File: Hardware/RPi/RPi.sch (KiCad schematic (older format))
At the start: 90 parts, among them P1 USB_B, P10 Solder_Pad, P11 Solder_Pad, P12 Solder_Pad, P13 Solder_Pad, P14 Solder_Pad, P15 Solder_Pad, P16 Solder_Pad, P17 Solder_Pad, P18 Solder_Pad, P2 USB_A, P3 USB_A, P4 USB_A, P5 USB_A, P6 Solder_Pad, P7 Solder_Pad, P8 Solder_Pad, P9 Solder_Pad, U1 AP1117E25, U10 WS2812B, U11 WS2812B, U12 WS2812B, U13 Teensy_LC, U14 WS2812B, U15 WS2812B, U16 WS2812B, U17 WS2812B, U18 WS2812B, U19 WS2812B, U2 Dual_buffer_NC7WZ16, U3 FE1.1s, U4 MPU_9150, U5 RPi_Interface, U6 ESP-12E, U7 WS2812B, U8 WS2812B, U9 WS2812B, Y1 Crystal 12MHz

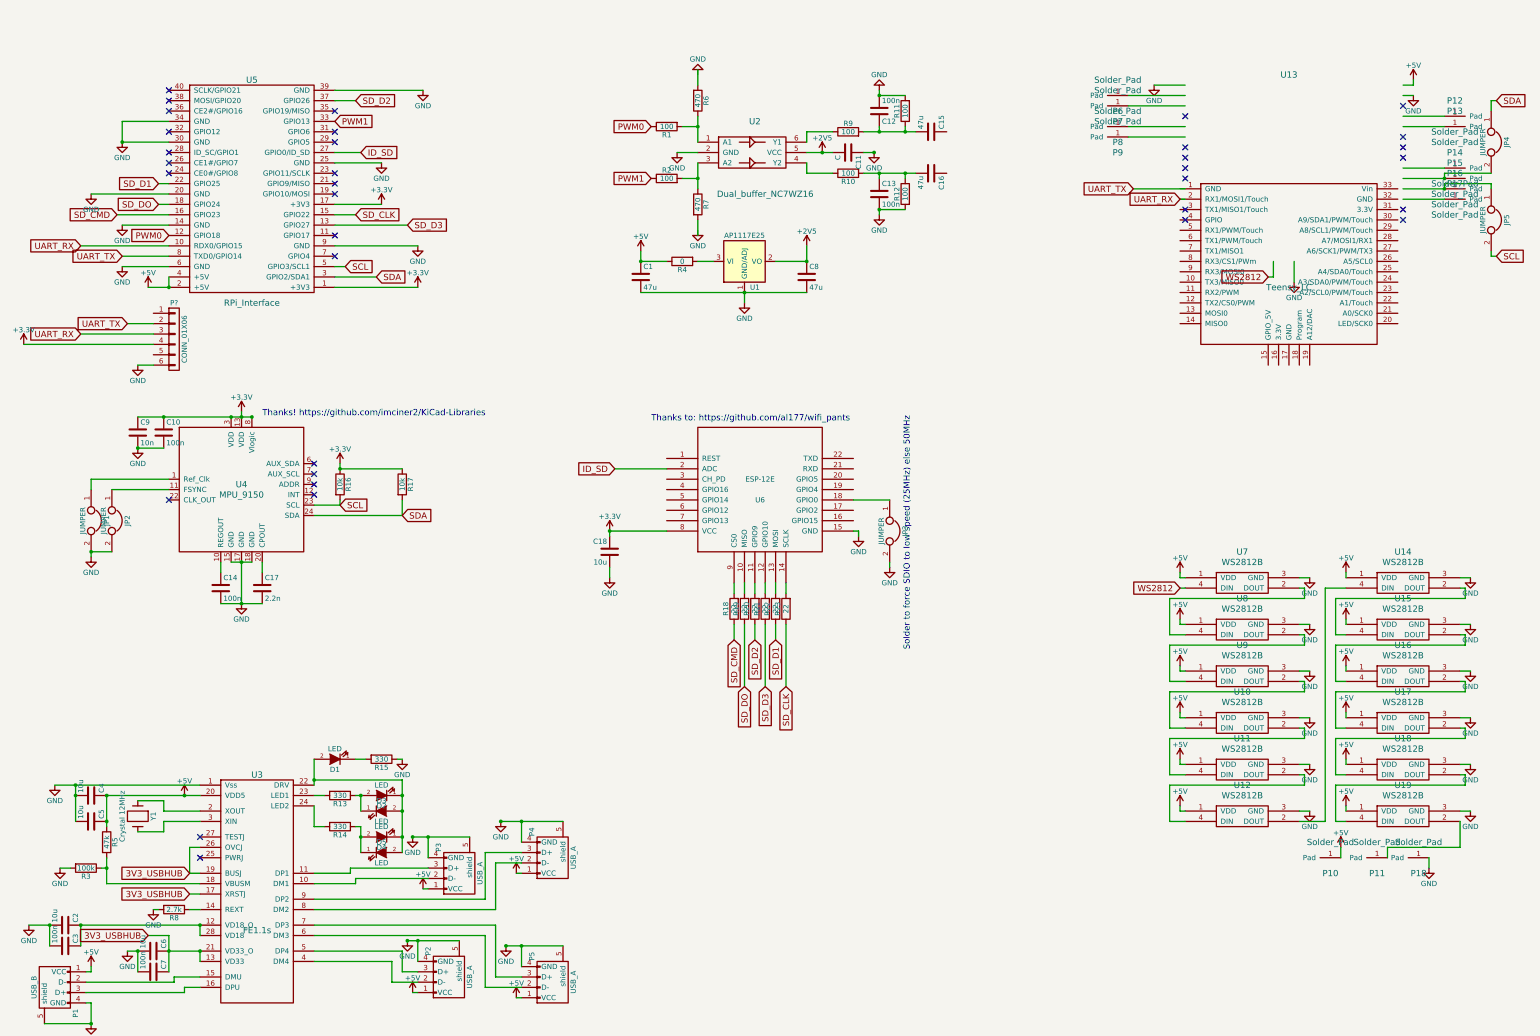
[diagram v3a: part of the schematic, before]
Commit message: Creating footprints
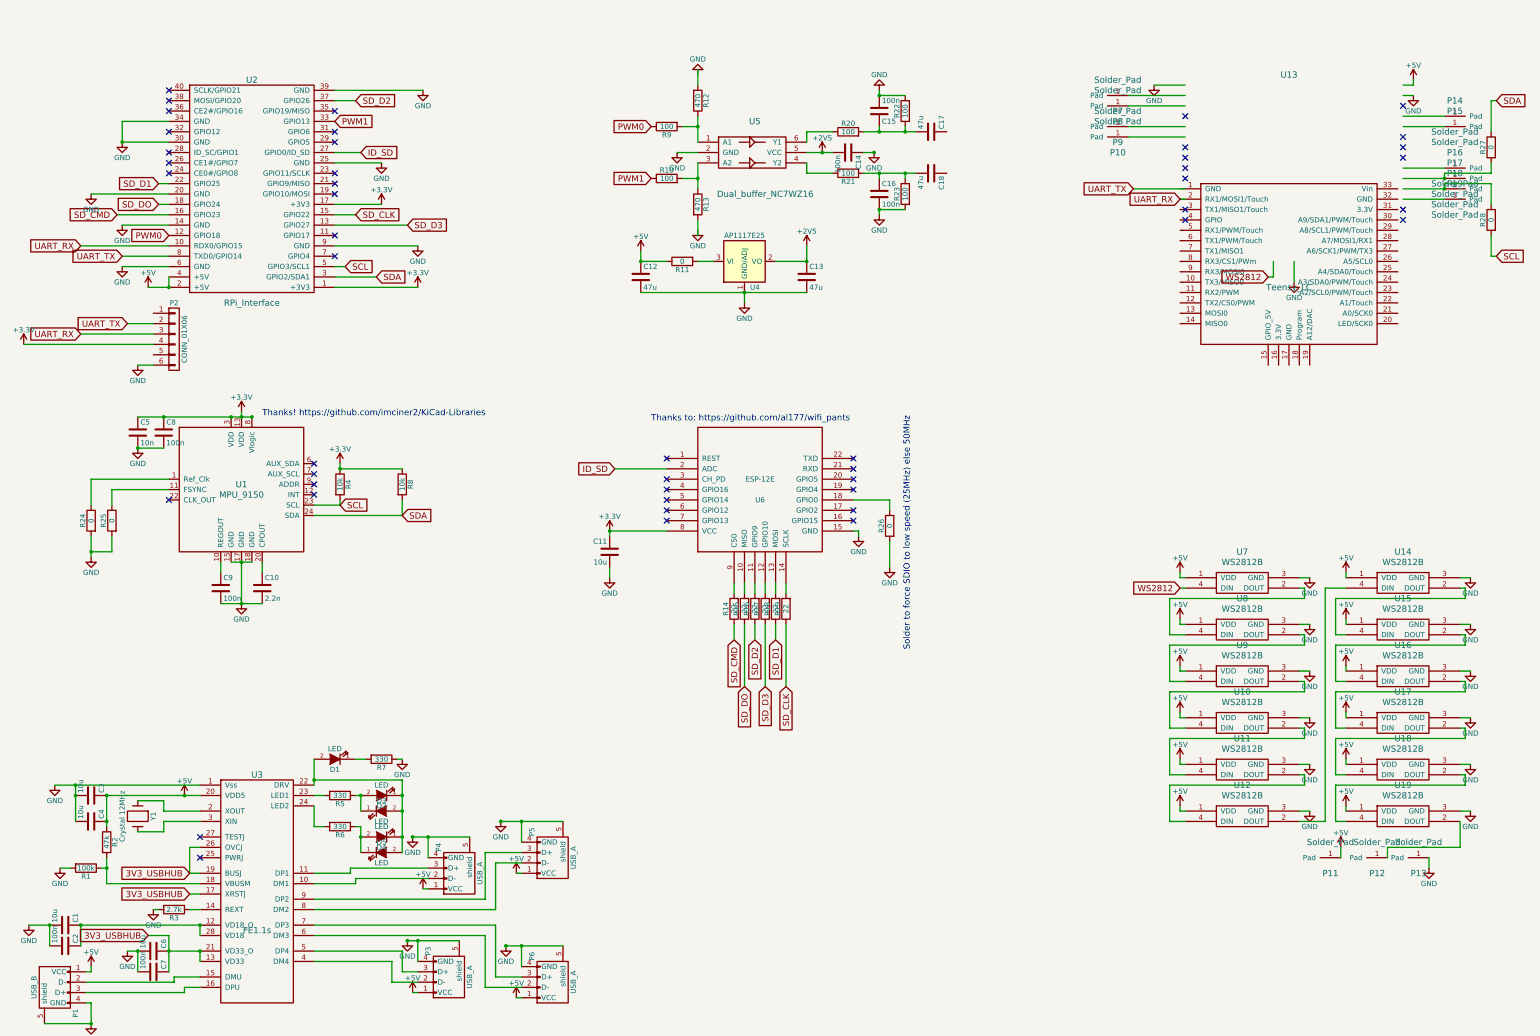
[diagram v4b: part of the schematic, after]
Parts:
- removed JP1, JP2, JP3, JP4, JP5: JUMPER, symbol JUMPER
- added R24, R25, R26, R27, R28: 0, Resistors_SMD:R_0603, symbol R
- C10: renamed from C17; footprint (none) -> Capacitors_SMD:C_0603
- C11: renamed from C18; footprint (none) -> Capacitors_SMD:C_0603
- C12: renamed from C1; footprint (none) -> Capacitors_SMD:C_0805
- C13: renamed from C8; footprint (none) -> Capacitors_SMD:C_0805
- C14: renamed from C11; value C -> 100n; footprint (none) -> Capacitors_SMD:C_0603
- C15: renamed from C12; footprint (none) -> Capacitors_SMD:C_0603
- C16: renamed from C13; footprint (none) -> Capacitors_SMD:C_0603
- C17: renamed from C15; footprint (none) -> Capacitors_SMD:C_0805
- C18: renamed from C16; footprint (none) -> Capacitors_SMD:C_0805
- C2: renamed from C3; footprint (none) -> Capacitors_SMD:C_0603
- C3: renamed from C4; footprint (none) -> Capacitors_SMD:C_0603
- C4: renamed from C5; footprint (none) -> Capacitors_SMD:C_0603
- C5: renamed from C9; footprint (none) -> Capacitors_SMD:C_0603
- C6, C7: footprint (none) -> Capacitors_SMD:C_0603
- C8: renamed from C10; footprint (none) -> Capacitors_SMD:C_0603
- C9: renamed from C14; footprint (none) -> Capacitors_SMD:C_0603
- D1, D2, D3, D4, D5: footprint (none) -> LEDs:LED_0603
- P1: footprint (none) -> Connect:USB_Mini-B
- P10: renamed from P9; footprint (none) -> Measurement_Points:Measurement_Point_Square-SMD-Pad_Big
- P11: renamed from P10; footprint (none) -> Measurement_Points:Measurement_Point_Square-SMD-Pad_Big
- P12: renamed from P11; footprint (none) -> Measurement_Points:Measurement_Point_Square-SMD-Pad_Big
- P13: renamed from P18; footprint (none) -> Measurement_Points:Measurement_Point_Square-SMD-Pad_Big
- P14: renamed from P12; footprint (none) -> Measurement_Points:Measurement_Point_Square-SMD-Pad_Big
- P15: renamed from P13; footprint (none) -> Measurement_Points:Measurement_Point_Square-SMD-Pad_Big
- P16: renamed from P14; footprint (none) -> Measurement_Points:Measurement_Point_Square-SMD-Pad_Big
- P17: renamed from P15; footprint (none) -> Measurement_Points:Measurement_Point_Square-SMD-Pad_Big
- P18: renamed from P16; footprint (none) -> Measurement_Points:Measurement_Point_Square-SMD-Pad_Big
- P19: renamed from P17; footprint (none) -> Measurement_Points:Measurement_Point_Square-SMD-Pad_Big
- P2: renamed from P?; footprint (none) -> TimeArc:1x06 pinheader smd
- P7: renamed from P6; footprint (none) -> Measurement_Points:Measurement_Point_Square-SMD-Pad_Big
- P8: renamed from P7; footprint (none) -> Measurement_Points:Measurement_Point_Square-SMD-Pad_Big
- P9: renamed from P8; footprint (none) -> Measurement_Points:Measurement_Point_Square-SMD-Pad_Big
- R1: renamed from R3; footprint (none) -> Resistors_SMD:R_0603
- R10: renamed from R2; footprint (none) -> Resistors_SMD:R_0603
- R11: renamed from R4; footprint (none) -> Resistors_SMD:R_0603
- R12: renamed from R6; footprint (none) -> Resistors_SMD:R_0603
- R13: renamed from R7; footprint (none) -> Resistors_SMD:R_0603
- R14: renamed from R18; footprint (none) -> Resistors_SMD:R_0603
- R15: renamed from R19; footprint (none) -> Resistors_SMD:R_0603
- R16: renamed from R20; footprint (none) -> Resistors_SMD:R_0603
- R17: renamed from R21; footprint (none) -> Resistors_SMD:R_0603
- R18: renamed from R22; footprint (none) -> Resistors_SMD:R_0603
- R19: renamed from R23; footprint (none) -> Resistors_SMD:R_0603
- R2: renamed from R5; footprint (none) -> Resistors_SMD:R_0603
- R20: renamed from R9; footprint (none) -> Resistors_SMD:R_0603
- R21: renamed from R10; footprint (none) -> Resistors_SMD:R_0603
- R22: renamed from R11; footprint (none) -> Resistors_SMD:R_0603
- R23: renamed from R12; footprint (none) -> Resistors_SMD:R_0603
- R3: renamed from R8; footprint (none) -> Resistors_SMD:R_0603
- R4: renamed from R16; footprint (none) -> Resistors_SMD:R_0603
- R5: renamed from R13; footprint (none) -> Resistors_SMD:R_0603
- R6: renamed from R14; footprint (none) -> Resistors_SMD:R_0603
- R7: renamed from R15; footprint (none) -> Resistors_SMD:R_0603
- R8: renamed from R17; footprint (none) -> Resistors_SMD:R_0603
- R9: renamed from R1; footprint (none) -> Resistors_SMD:R_0603
- U1: renamed from U4; footprint (none) -> TimeArc:IMU9150
- renumbered C2 to C1, P2 to P3, P3 to P4, P4 to P5, P5 to P6, U5 to U2, U1 to U4, U2 to U5
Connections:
- wire segments 311 -> 315
- no-connect marks 35 -> 47

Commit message: New hardware ideas
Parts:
- U10, U11, U12, U14, U15, U16, U17, U18, U19, U7, U8, U9: footprint (none) -> ws2812:PLCC4-5050
- U2: footprint (none) -> TimeArc:RPi_Zero_farnell_1256663
- U3: footprint (none) -> Housings_SSOP:SSOP-28_5.3x10.2mm_Pitch0.65mm
- U4: footprint (none) -> TO_SOT_Packages_SMD:SOT-223
- U5: footprint (none) -> TO_SOT_Packages_SMD:SC-70
- U6: footprint (none) -> ESP8266:ESP-12E
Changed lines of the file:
@@
 F 0 "U5" H 7950 2150 60  0000 C CNN
 F 1 "Dual_buffer_NC7WZ16" H 8050 1450 60  0000 C CNN
-F 2 "" H 7700 1800 60  0001 C CNN
+F 2 "TO_SOT_Packages_SMD:SC-70" H 7700 1800 60  0001 C CNN
 F 3 "" H 7700 1800 60  0000 C CNN
 	1    7900 1800
@@
 F 0 "U2" H 3100 3050 60  0000 C CNN
 F 1 "RPi_Interface" H 3100 900 60  0000 C CNN
-F 2 "" H 3050 1650 60  0001 C CNN
+F 2 "TimeArc:RPi_Zero_farnell_1256663" H 3050 1650 60  0001 C CNN
 F 3 "" H 3050 1650 60  0000 C CNN
 	1    3100 2050
@@
 F 0 "U4" H 7950 2550 50  0000 C CNN
 F 1 "AP1117E25" H 7850 3050 50  0000 C CNN
-F 2 "" H 7850 2800 50  0001 C CNN
+F 2 "TO_SOT_Packages_SMD:SOT-223" H 7850 2800 50  0001 C CNN
 F 3 "" H 7850 2800 50  0000 C CNN
 	1    7850 2800
@@
 F 0 "U3" H 3150 9250 60  0000 C CNN
 F 1 "FE1.1s" H 3150 7750 60  0000 C CNN
-F 2 "" H 3200 8200 60  0001 C CNN
+F 2 "Housings_SSOP:SSOP-28_5.3x10.2mm_Pitch0.65mm" H 3200 8200 60  0001 C CNN
 F 3 "" H 3200 8200 60  0000 C CNN
 	1    3150 8500
@@
 F 0 "U6" H 8000 4900 50  0000 C CNN
 F 1 "ESP-12E" H 8000 5100 50  0000 C CNN
-F 2 "" H 8000 5000 50  0001 C CNN
+F 2 "ESP8266:ESP-12E" H 8000 5000 50  0001 C CNN
 F 3 "" H 8000 5000 50  0001 C CNN
 	1    8000 5000
@@
 F 0 "U9" H 12650 6700 60  0000 C CNN
 F 1 "WS2812B" H 12650 6600 60  0000 C CNN
-F 2 "" H 12650 6600 60  0001 C CNN
+F 2 "ws2812:PLCC4-5050" H 12650 6600 60  0001 C CNN
 F 3 "" H 12650 6600 60  0000 C CNN
 	1    12650 6600
@@
 F 0 "U10" H 12650 7150 60  0000 C CNN
 F 1 "WS2812B" H 12650 7050 60  0000 C CNN
-F 2 "" H 12650 7050 60  0001 C CNN
+F 2 "ws2812:PLCC4-5050" H 12650 7050 60  0001 C CNN
 F 3 "" H 12650 7050 60  0000 C CNN
 	1    12650 7050
@@
 F 0 "U7" H 12650 5800 60  0000 C CNN
 F 1 "WS2812B" H 12650 5700 60  0000 C CNN
-F 2 "" H 12650 5700 60  0001 C CNN
+F 2 "ws2812:PLCC4-5050" H 12650 5700 60  0001 C CNN
 F 3 "" H 12650 5700 60  0000 C CNN
 	1    12650 5700
@@
 F 0 "U8" H 12650 6250 60  0000 C CNN
 F 1 "WS2812B" H 12650 6150 60  0000 C CNN
-F 2 "" H 12650 6150 60  0001 C CNN
+F 2 "ws2812:PLCC4-5050" H 12650 6150 60  0001 C CNN
 F 3 "" H 12650 6150 60  0000 C CNN
 	1    12650 6150
@@
 F 0 "U14" H 14200 5800 60  0000 C CNN
 F 1 "WS2812B" H 14200 5700 60  0000 C CNN
-F 2 "" H 14200 5700 60  0001 C CNN
+F 2 "ws2812:PLCC4-5050" H 14200 5700 60  0001 C CNN
 F 3 "" H 14200 5700 60  0000 C CNN
 	1    14200 5700
@@
 F 0 "U15" H 14200 6250 60  0000 C CNN
 F 1 "WS2812B" H 14200 6150 60  0000 C CNN
-F 2 "" H 14200 6150 60  0001 C CNN
+F 2 "ws2812:PLCC4-5050" H 14200 6150 60  0001 C CNN
 F 3 "" H 14200 6150 60  0000 C CNN
 	1    14200 6150
@@
 F 0 "U11" H 12650 7600 60  0000 C CNN
 F 1 "WS2812B" H 12650 7500 60  0000 C CNN
-F 2 "" H 12650 7500 60  0001 C CNN
+F 2 "ws2812:PLCC4-5050" H 12650 7500 60  0001 C CNN
 F 3 "" H 12650 7500 60  0000 C CNN
 	1    12650 7500
@@
 F 0 "U12" H 12650 8050 60  0000 C CNN
 F 1 "WS2812B" H 12650 7950 60  0000 C CNN
-F 2 "" H 12650 7950 60  0001 C CNN
+F 2 "ws2812:PLCC4-5050" H 12650 7950 60  0001 C CNN
 F 3 "" H 12650 7950 60  0000 C CNN
 	1    12650 7950
@@
 F 0 "U16" H 14200 6700 60  0000 C CNN
 F 1 "WS2812B" H 14200 6600 60  0000 C CNN
-F 2 "" H 14200 6600 60  0001 C CNN
+F 2 "ws2812:PLCC4-5050" H 14200 6600 60  0001 C CNN
 F 3 "" H 14200 6600 60  0000 C CNN
 	1    14200 6600
@@
 F 0 "U19" H 14200 8050 60  0000 C CNN
 F 1 "WS2812B" H 14200 7950 60  0000 C CNN
-F 2 "" H 14200 7950 60  0001 C CNN
+F 2 "ws2812:PLCC4-5050" H 14200 7950 60  0001 C CNN
 F 3 "" H 14200 7950 60  0000 C CNN
 	1    14200 7950
@@
 F 0 "U17" H 14200 7150 60  0000 C CNN
 F 1 "WS2812B" H 14200 7050 60  0000 C CNN
-F 2 "" H 14200 7050 60  0001 C CNN
+F 2 "ws2812:PLCC4-5050" H 14200 7050 60  0001 C CNN
 F 3 "" H 14200 7050 60  0000 C CNN
 	1    14200 7050
@@
 F 0 "U18" H 14200 7600 60  0000 C CNN
 F 1 "WS2812B" H 14200 7500 60  0000 C CNN
-F 2 "" H 14200 7500 60  0001 C CNN
+F 2 "ws2812:PLCC4-5050" H 14200 7500 60  0001 C CNN
 F 3 "" H 14200 7500 60  0000 C CNN
 	1    14200 7500

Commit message: netlist update
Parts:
- C1: footprint (none) -> Capacitors_SMD:C_0603
- P3, P4, P5, P6: footprint (none) -> TimeArc:USB_A_SMD_Pads
- U13: footprint (none) -> TimeArc:TeensyLC
- Y1: footprint (none) -> TimeArc:Crystal_12MHz
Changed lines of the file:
@@
 F 0 "Y1" H 2000 8300 50  0000 C CNN
 F 1 "Crystal 12MHz" H 2000 8000 50  0000 C CNN
-F 2 "" H 2000 8150 50  0001 C CNN
+F 2 "TimeArc:Crystal_12MHz" H 2000 8150 50  0001 C CNN
 F 3 "" H 2000 8150 50  0000 C CNN
 	1    2000 8150
@@
 F 0 "C1" H 1325 9300 50  0000 L CNN
 F 1 "10u" H 1325 9100 50  0000 L CNN
-F 2 "" H 1338 9050 50  0001 C CNN
+F 2 "Capacitors_SMD:C_0603" H 1338 9050 50  0001 C CNN
 F 3 "" H 1300 9200 50  0000 C CNN
 	1    1300 9200
@@
 F 0 "P4" H 5300 8450 50  0000 C CNN
 F 1 "USB_A" H 5050 8850 50  0000 C CNN
-F 2 "" V 5050 8550 50  0001 C CNN
+F 2 "TimeArc:USB_A_SMD_Pads" V 5050 8550 50  0001 C CNN
 F 3 "" V 5050 8550 50  0000 C CNN
 	1    5100 8650
@@
 F 0 "P3" H 5200 9450 50  0000 C CNN
 F 1 "USB_A" H 4950 9850 50  0000 C CNN
-F 2 "" V 4950 9550 50  0001 C CNN
+F 2 "TimeArc:USB_A_SMD_Pads" V 4950 9550 50  0001 C CNN
 F 3 "" V 4950 9550 50  0000 C CNN
 	1    5000 9650
@@
 F 0 "P5" H 6200 8300 50  0000 C CNN
 F 1 "USB_A" H 5950 8700 50  0000 C CNN
-F 2 "" V 5950 8400 50  0001 C CNN
+F 2 "TimeArc:USB_A_SMD_Pads" V 5950 8400 50  0001 C CNN
 F 3 "" V 5950 8400 50  0000 C CNN
 	1    6000 8500
@@
 F 0 "P6" H 6200 9500 50  0000 C CNN
 F 1 "USB_A" H 5950 9900 50  0000 C CNN
-F 2 "" V 5950 9600 50  0001 C CNN
+F 2 "TimeArc:USB_A_SMD_Pads" V 5950 9600 50  0001 C CNN
 F 3 "" V 5950 9600 50  0000 C CNN
 	1    6000 9700
@@
 F 0 "U13" H 13100 3600 60  0000 C CNN
 F 1 "Teensy_LC" H 13100 1550 60  0000 C CNN
-F 2 "" H 13100 2300 60  0001 C CNN
+F 2 "TimeArc:TeensyLC" H 13100 2300 60  0001 C CNN
 F 3 "" H 13100 2300 60  0000 C CNN
 	1    13100 2300
